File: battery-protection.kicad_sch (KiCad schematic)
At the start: 8 parts, among them Q3 Q_PMOS_GSD, Q4 Q_PMOS_GSD

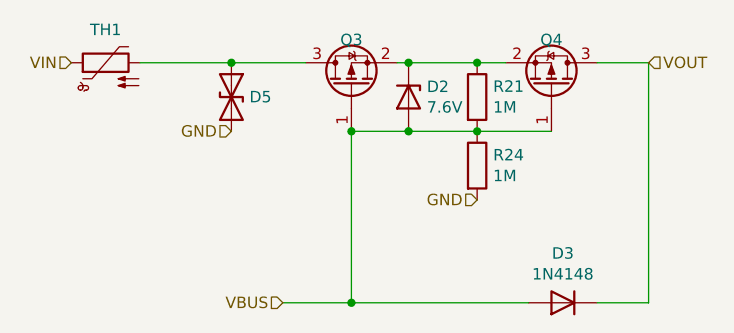
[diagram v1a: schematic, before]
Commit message: New kicad formats. Mark holes and fiducials and other DNP components as non-bom, update values for transistors and diodes
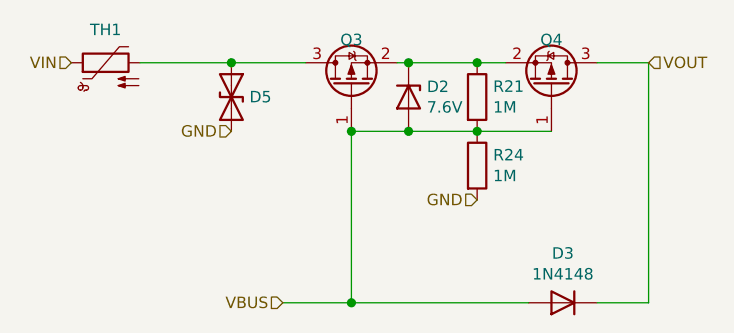
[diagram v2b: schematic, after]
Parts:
- D5: value D_TVS -> SMF11A
- Q3, Q4: value Q_PMOS_GSD -> NX2301P
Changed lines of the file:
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@@
-(kicad_sch (version 20200512) (host eeschema "5.99.0-unknown-eae0c14~88~ubuntu18.04.1")
+(kicad_sch (version 20200828) (generator eeschema)
   (page 2 5)
   (paper "A4")
-  (junction (at 55.245 45.72))
-  (junction (at 68.58 53.34))
-  (junction (at 68.58 72.39))
-  (junction (at 74.93 45.72))
-  (junction (at 74.93 53.34))
-  (junction (at 82.55 45.72))
-  (junction (at 82.55 53.34))
+  (junction (at 55.245 45.72) (diameter 1.016) (color 0 0 0 0))
+  (junction (at 68.58 53.34) (diameter 1.016) (color 0 0 0 0))
+  (junction (at 68.58 72.39) (diameter 1.016) (color 0 0 0 0))
+  (junction (at 74.93 45.72) (diameter 1.016) (color 0 0 0 0))
+  (junction (at 74.93 53.34) (diameter 1.016) (color 0 0 0 0))
+  (junction (at 82.55 45.72) (diameter 1.016) (color 0 0 0 0))
+  (junction (at 82.55 53.34) (diameter 1.016) (color 0 0 0 0))
   (wire (pts (xy 45.085 45.72) (xy 55.245 45.72))
     (stroke (width 0) (type solid) (color 0 0 0 0))
@@
   )
   (symbol (lib_id "Device:R") (at 82.55 49.53 0) (unit 1)
+    (in_bom yes) (on_board yes)
     (property "Reference" "R21" (id 0) (at 84.328 48.3616 0)
       (effects (font (size 1.27 1.27)) (justify left))
@@
   )
   (symbol (lib_id "Device:R") (at 82.55 57.15 0) (unit 1)
+    (in_bom yes) (on_board yes)
     (property "Reference" "R24" (id 0) (at 84.328 55.9816 0)
       (effects (font (size 1.27 1.27)) (justify left))
@@
   )
   (symbol (lib_id "Device:D_TVS") (at 55.245 49.53 270) (unit 1)
+    (in_bom yes) (on_board yes)
     (property "Reference" "D5" (id 0) (at 57.2516 49.53 90)
       (effects (font (size 1.27 1.27)) (justify left))
     )
-    (property "Value" "D_TVS" (id 1) (at 57.2516 50.673 90)
+    (property "Value" "SMF11A" (id 1) (at 57.2516 50.673 90)
       (effects (font (size 1.27 1.27)) (justify left) hide)
     )
@@
   )
   (symbol (lib_id "Device:D_Zener") (at 74.93 49.53 270) (unit 1)
+    (in_bom yes) (on_board yes)
     (property "Reference" "D2" (id 0) (at 76.962 48.387 90)
       (effects (font (size 1.27 1.27)) (justify left))
@@
   )
   (symbol (lib_id "Device:D") (at 92.075 72.39 180) (unit 1)
+    (in_bom yes) (on_board yes)
     (property "Reference" "D3" (id 0) (at 92.075 66.9036 0))
     (property "Value" "1N4148" (id 1) (at 92.075 69.215 0))
@@
   )
   (symbol (lib_id "Device:Thermistor_PTC") (at 41.275 45.72 90) (unit 1)
+    (in_bom yes) (on_board yes)
     (property "Reference" "TH1" (id 0) (at 41.275 42.0624 90))
     (property "Value" "Thermistor_PTC" (id 1) (at 41.275 42.0624 90)
@@
   )
   (symbol (lib_id "Device:Q_PMOS_GSD") (at 68.58 48.26 90) (unit 1)
+    (in_bom yes) (on_board yes)
     (property "Reference" "Q3" (id 0) (at 68.58 43.18 90))
-    (property "Value" "Q_PMOS_GSD" (id 1) (at 68.58 42.2402 90)
+    (property "Value" "NX2301P" (id 1) (at 68.58 42.2402 90)
       (effects (font (size 1.27 1.27)) hide)
     )
@@
   )
   (symbol (lib_id "Device:Q_PMOS_GSD") (at 90.805 48.26 270) (mirror x) (unit 1)
+    (in_bom yes) (on_board yes)
     (property "Reference" "Q4" (id 0) (at 90.805 43.18 90))
-    (property "Value" "Q_PMOS_GSD" (id 1) (at 90.805 42.2402 90)
-      (effects (font (size 1.27 1.27)) hide)
-    )
+    (property "Value" "NX2301P" (id 1) (at 90.805 42.2402 90)
+      (effects (font (size 1.27 1.27)) hide)
+    )

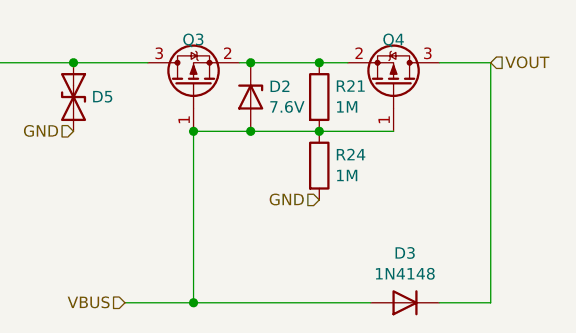
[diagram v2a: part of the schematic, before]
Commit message: Update PCB:  * Update shape so it fits into case  * Update most of the components for JLCPCB assembly
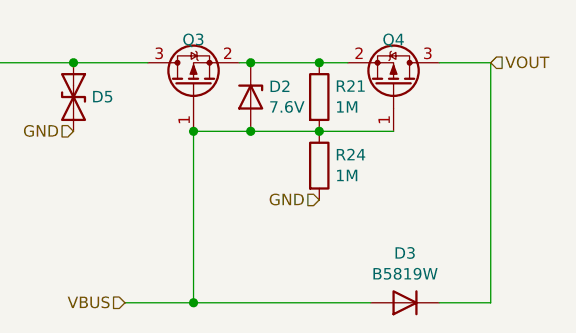
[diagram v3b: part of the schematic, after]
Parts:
- D2: LCSC (none) -> C118605
- D3: value 1N4148 -> B5819W; LCSC (none) -> C8598
- D5: LCSC (none) -> C169335
- Q3, Q4: LCSC (none) -> C10487
- R21, R24: LCSC (none) -> C22935
- TH1: LCSC (none) -> C70079
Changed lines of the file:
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@@
-(kicad_sch (version 20200828) (generator eeschema)
-  (page 2 5)
+(kicad_sch (version 20201015) (generator eeschema)
+  (page 1 5)
   (paper "A4")
   (junction (at 55.245 45.72) (diameter 1.016) (color 0 0 0 0))
@@
       (effects (font (size 1.27 1.27)) hide)
     )
+    (property "LCSC" "C22935" (id 4) (at 82.55 49.53 0)
+      (effects (font (size 1.27 1.27)) hide)
+    )
   )
   (symbol (lib_id "Device:R") (at 82.55 57.15 0) (unit 1)
@@
     )
     (property "Datasheet" "~" (id 3) (at 82.55 57.15 0)
+      (effects (font (size 1.27 1.27)) hide)
+    )
+    (property "LCSC" "C22935" (id 4) (at 82.55 57.15 0)
       (effects (font (size 1.27 1.27)) hide)
     )
@@
       (effects (font (size 1.27 1.27)) hide)
     )
+    (property "LCSC" "C169335" (id 4) (at 55.245 49.53 0)
+      (effects (font (size 1.27 1.27)) hide)
+    )
   )
   (symbol (lib_id "Device:D_Zener") (at 74.93 49.53 270) (unit 1)
@@
       (effects (font (size 1.27 1.27)) hide)
     )
+    (property "LCSC" "C118605" (id 4) (at 74.93 49.53 0)
+      (effects (font (size 1.27 1.27)) hide)
+    )
   )
   (symbol (lib_id "Device:D") (at 92.075 72.39 180) (unit 1)
     (in_bom yes) (on_board yes)
     (property "Reference" "D3" (id 0) (at 92.075 66.9036 0))
-    (property "Value" "1N4148" (id 1) (at 92.075 69.215 0))
+    (property "Value" "B5819W" (id 1) (at 92.075 69.215 0))
     (property "Footprint" "Diode_SMD:D_SOD-123" (id 2) (at 92.075 72.39 0)
       (effects (font (size 1.27 1.27)) hide)
@@
     )
     (property "PartNo" "1N4148W-7-F" (id 5) (at 92.075 72.39 0)
+      (effects (font (size 1.27 1.27)) hide)
+    )
+    (property "LCSC" "C8598" (id 4) (at 92.075 72.39 0)
       (effects (font (size 1.27 1.27)) hide)
     )
@@
       (effects (font (size 1.27 1.27)) hide)
     )
+    (property "LCSC" "C70079" (id 4) (at 41.275 45.72 0)
+      (effects (font (size 1.27 1.27)) hide)
+    )
   )
   (symbol (lib_id "Device:Q_PMOS_GSD") (at 68.58 48.26 90) (unit 1)
@@
       (effects (font (size 1.27 1.27)) hide)
     )
+    (property "LCSC" "C10487" (id 4) (at 68.58 48.26 0)
+      (effects (font (size 1.27 1.27)) hide)
+    )
   )
   (symbol (lib_id "Device:Q_PMOS_GSD") (at 90.805 48.26 270) (mirror x) (unit 1)
@@
       (effects (font (size 1.27 1.27)) hide)
     )
+    (property "LCSC" "C10487" (id 4) (at 90.805 48.26 0)
+      (effects (font (size 1.27 1.27)) hide)
+    )

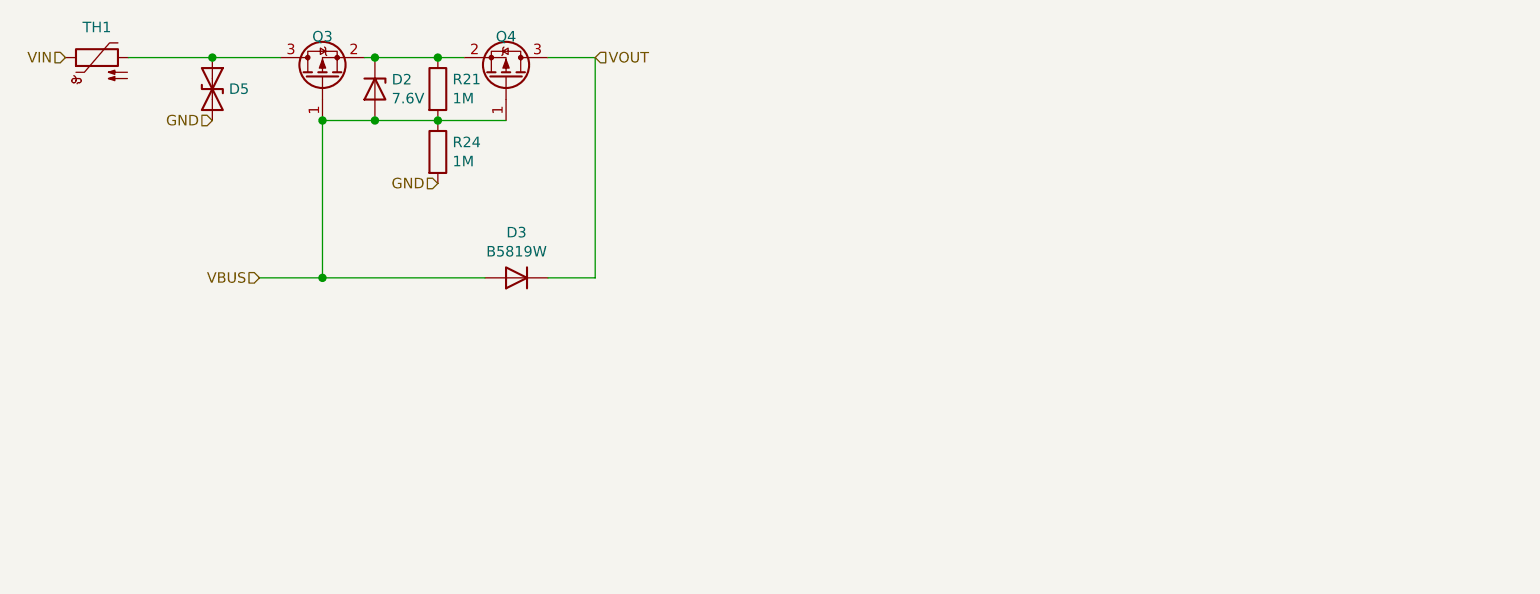
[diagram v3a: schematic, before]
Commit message: Fix ESD diode symbol and routing. Update reset/boot0 circuit to one that works satisfactory
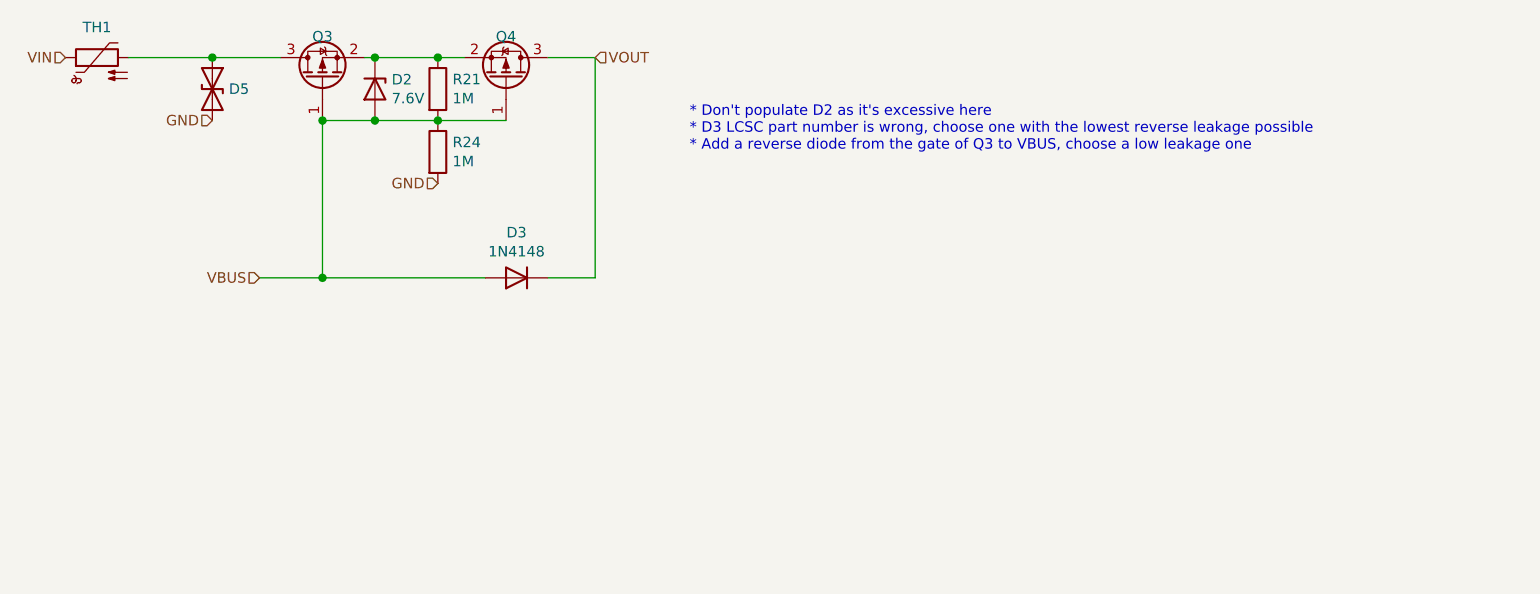
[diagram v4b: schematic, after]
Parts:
- D3: value B5819W -> 1N4148
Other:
- note added: "* Don't populate D2 as it's excessive here * D3 LCSC part number is wrong, choose one with the lowest reverse leakage possible * Add a reverse diode from the gate of Q3 to VBUS, choose a low leakage one"

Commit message: Set proper LCSC numbers to components, consolidate some values
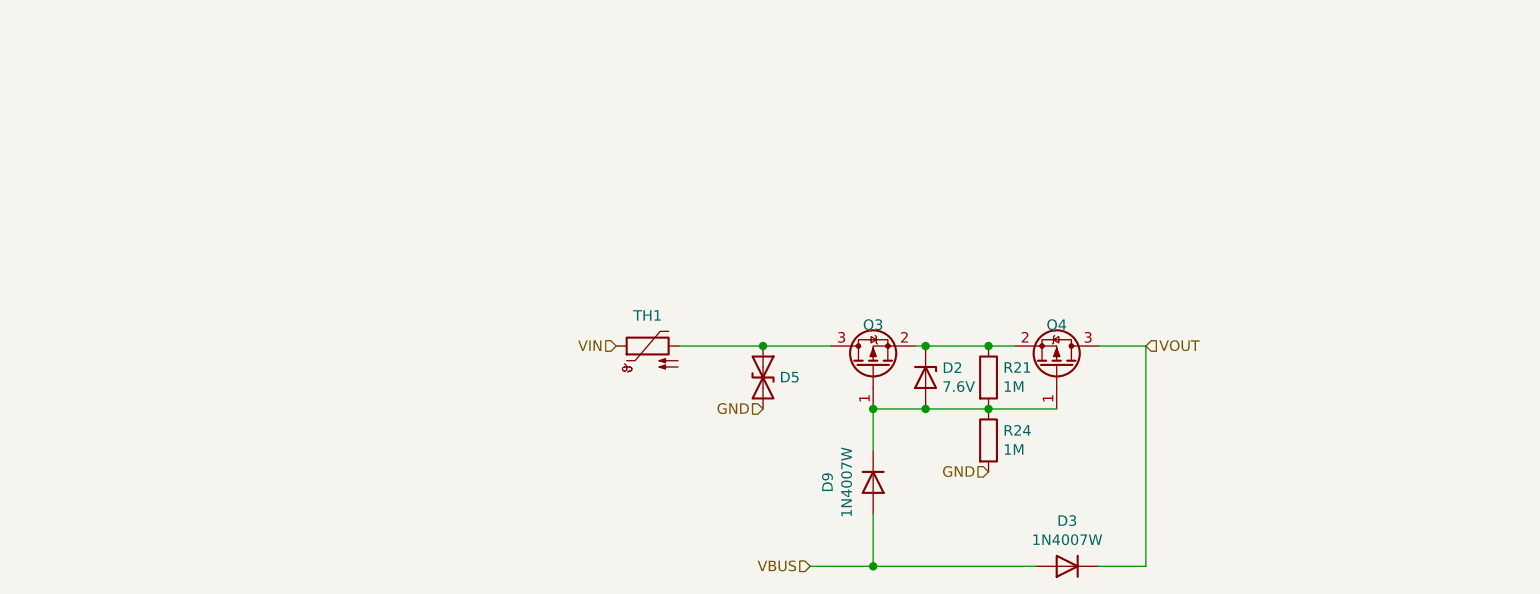
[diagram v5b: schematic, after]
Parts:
- added D9: 1N4007W, Diode_SMD:D_SOD-123F, symbol Device:D
- D2: DNP (none) -> DNP; LCSC C118605 -> (none)
- D3: value 1N4148 -> 1N4007W; footprint Diode_SMD:D_SOD-123 -> Diode_SMD:D_SOD-123F; LCSC C8598 -> C108803
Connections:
- net VBUS: now also D9.2 (A); no longer D2.2 (A), Q3.1 (G), Q4.1 (G), R21.2, R24.1
- new net: D2.2 (A), D9.1 (K), Q3.1 (G), Q4.1 (G), R21.2, R24.1
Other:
- note removed: "* Don't populate D2 as it's excessive here * D3 LCSC part number is wrong, choose one with the lowest reverse leakage possible * Add a reverse diode from the gate of Q3 to VBUS, choose a low leakage one"
- moved on the sheet: D2, D3, D5, Q3, Q4, R21, R24, TH1
